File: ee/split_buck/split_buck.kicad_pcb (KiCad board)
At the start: 2 copper layers, 21.6 x 34.3 mm, 13 parts, among them J1 Conn_01x08, J3 Conn_01x03, Q1 DMP2160U

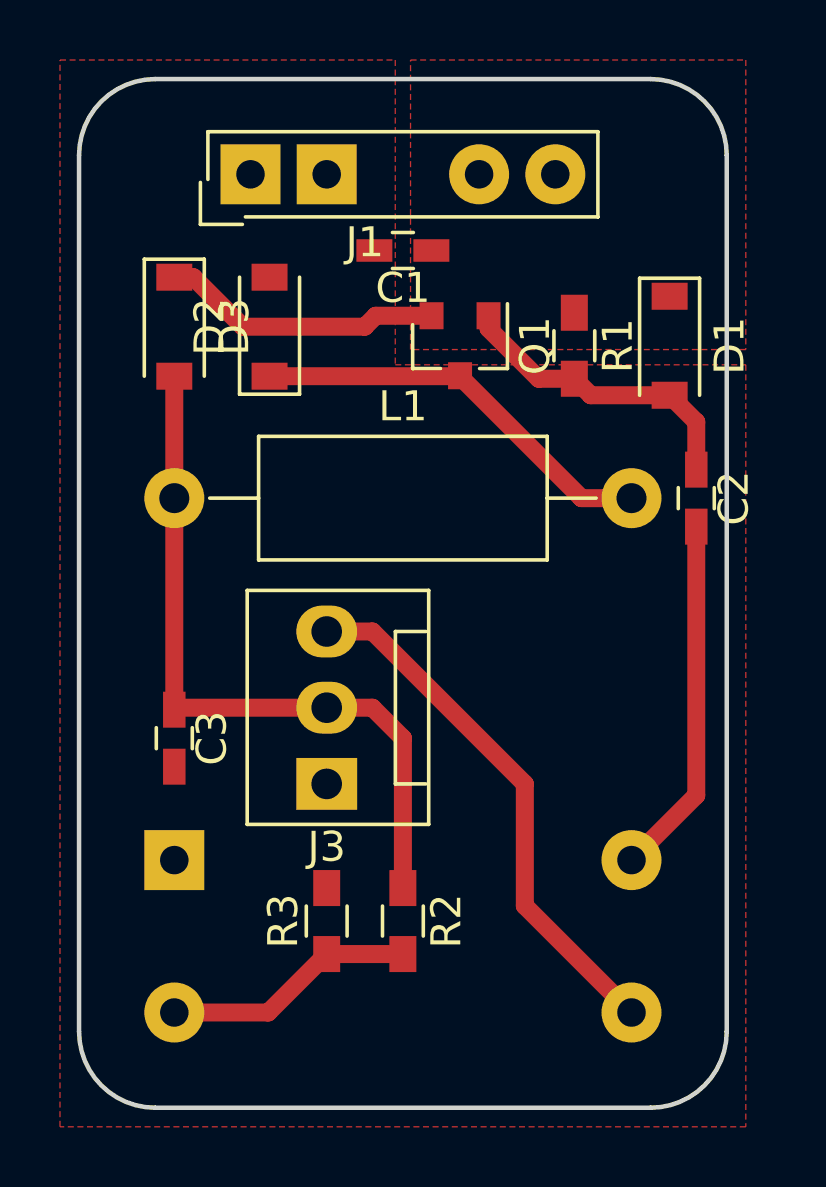
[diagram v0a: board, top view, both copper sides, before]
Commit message: Update split_buck design
- switched D1 to zener to protect FET Vgs
- increased input/output caps from 1u to 10u (0603 -> 0805)
- rotated fan header 30degrees to enable multiple channels
- added net names
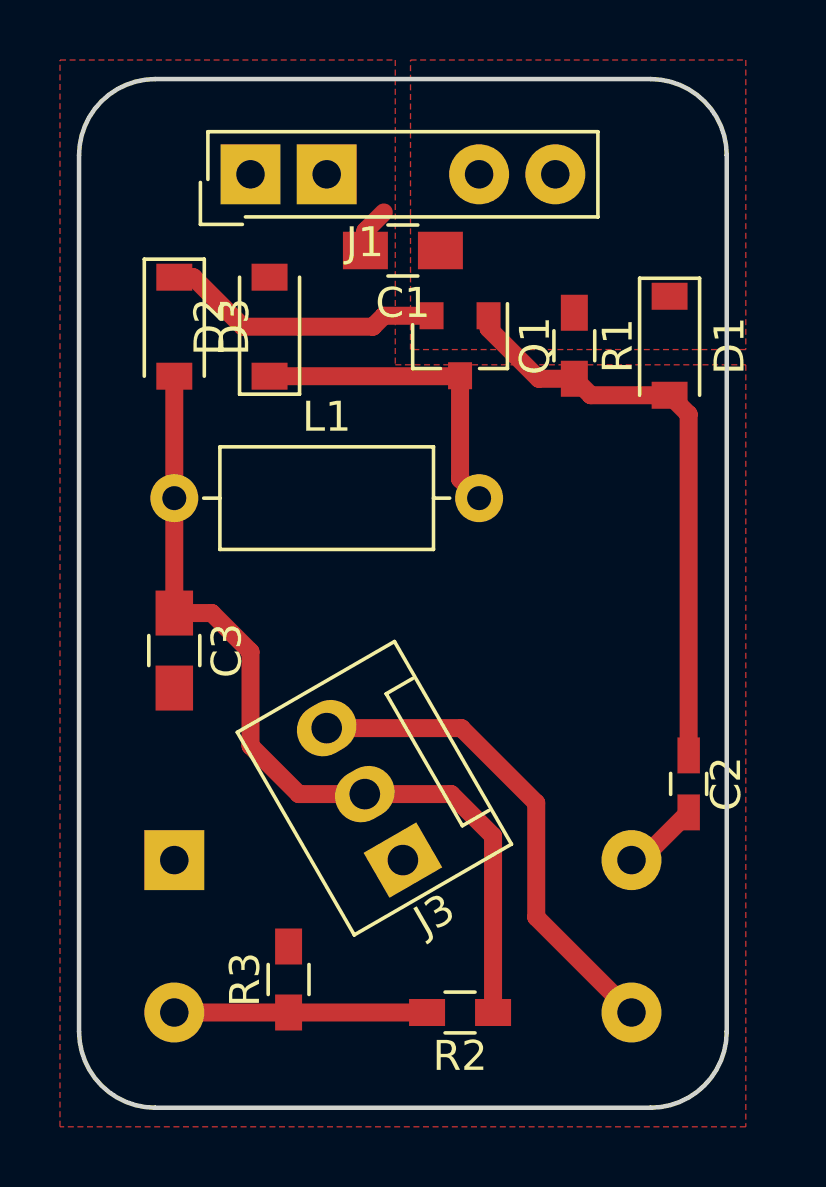
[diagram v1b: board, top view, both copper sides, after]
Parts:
- C1, C3: value 1u -> 10u; footprint Capacitors_SMD:C_0603_HandSoldering -> Capacitors_SMD:C_0805_HandSoldering
- D1: value D_Schottky -> D_Zener
- L1: footprint Inductors_THT:L_Axial_L9.5mm_D4.0mm_P15.24mm_Horizontal_Fastron_SMCC -> Inductors_THT:L_Axial_L7.0mm_D3.3mm_P10.16mm_Horizontal_Fastron_MICC
- moved C2 9.53 mm to (21.0, 24.1)
- moved R2 3.59 mm to (13.3, 31.8), turned to 180 degrees
- moved J3 3.59 mm to (11.4, 26.7), turned to 210 degrees
- moved C3 2.92 mm to (3.81, 19.7)
- moved R3 2.33 mm to (7.62, 30.6)
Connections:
- net Net-(C2-Pad1) renamed /GATE
- net Net-(C3-Pad1) renamed /FAN_VOUT
- net Net-(D2-Pad1) renamed /IND_SW
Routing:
- net /FAN_CTRL: track 12.0 -> 2.56 mm
- net /GATE: track 10.2 -> 19.7 mm
- net /FAN_VOUT: track 24.2 -> 29.3 mm
- net /IND_SW: track 13.7 -> 10.7 mm
- net GND: track 0.00 -> 1.52 mm
- net /FAN_RPM: track 17.8 -> 16.3 mm

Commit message: fine tune layout for othermill
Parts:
- moved D1 0.64 mm to (19.7, 9.53)
- moved D2 0.38 mm to (7.37, 8.89)
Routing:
- net +12V: track 9.54 -> 11.8 mm
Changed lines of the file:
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@@
     (links 26)
     (no_connects 1)
-    (area 0.559999 0.559999 22.300001 35.000001)
+    (area -0.475001 -0.475001 23.48 36.035001)
     (thickness 1.6)
     (drawings 8)
-    (tracks 37)
+    (tracks 42)
     (zones 0)
     (modules 13)
@@
   )
   (module Diodes_SMD:D_SOD-123 placed (layer F.Cu)
-    (at 20.32 9.525 270)
+    (at 19.685 9.525 270)
     (descr SOD-123)
     (tags SOD-123)
@@
   )
   (module Diodes_SMD:D_SOD-123 placed (layer F.Cu)
-    (at 6.985 8.89 90)
+    (at 7.366 8.89 90)
     (descr SOD-123)
     (tags SOD-123)
@@
   (gr_arc (start 19.685 3.175) (end 19.685 0.635) (angle 90) (layer Edge.Cuts) (width 0.15))
   (gr_arc (start 3.175 3.175) (end 0.635 3.175) (angle 90) (layer Edge.Cuts) (width 0.15))
+  (segment (start 12.385 8.525) (end 12.385 6.645) (width 0.6) (layer F.Cu) (net 1))
+  (segment (start 12.385 6.645) (end 12.68 6.35) (width 0.6) (layer F.Cu) (net 1))
   (segment (start 3.81 7.24) (end 4.446 7.24) (width 0.6) (layer F.Cu) (net 1))
   (segment (start 10.795 8.525) (end 12.385 8.525) (width 0.6) (layer F.Cu) (net 1))
@@
   (segment (start 12.235 31.75) (end 7.62 31.75) (width 0.6) (layer F.Cu) (net 3))
   (segment (start 3.81 31.75) (end 7.62 31.75) (width 0.6) (layer F.Cu) (net 3))
-  (segment (start 8.89 22.270591) (end 13.380591 22.270591) (width 0.6) (layer F.Cu) (net 4))
+  (segment (start 8.89 22.270591) (end 12.872591 22.270591) (width 0.6) (layer F.Cu) (net 4) (status 400000))
   (segment (start 15.875 28.575) (end 19.05 31.75) (width 0.6) (layer F.Cu) (net 4))
-  (segment (start 15.875 24.765) (end 15.875 28.575) (width 0.6) (layer F.Cu) (net 4))
-  (segment (start 13.380591 22.270591) (end 15.875 24.765) (width 0.6) (layer F.Cu) (net 4))
+  (segment (start 15.875 25.273) (end 15.875 28.575) (width 0.6) (layer F.Cu) (net 4))
+  (segment (start 12.872591 22.270591) (end 15.875 25.273) (width 0.6) (layer F.Cu) (net 4))
   (segment (start 19.05 26.67) (end 19.365 26.67) (width 0.6) (layer F.Cu) (net 5))
   (segment (start 19.365 26.67) (end 20.955 25.08) (width 0.6) (layer F.Cu) (net 5))
-  (segment (start 20.955 23.18) (end 20.955 11.81) (width 0.6) (layer F.Cu) (net 6))
-  (segment (start 20.955 11.81) (end 20.32 11.175) (width 0.6) (layer F.Cu) (net 6))
+  (segment (start 20.955 23.18) (end 20.955 22.733) (width 0.6) (layer F.Cu) (net 6))
+  (segment (start 20.955 22.733) (end 21.209 22.479) (width 0.6) (layer F.Cu) (net 6))
+  (segment (start 21.209 22.479) (end 21.209 12.064) (width 0.6) (layer F.Cu) (net 6))
+  (segment (start 21.209 12.064) (end 20.32 11.175) (width 0.6) (layer F.Cu) (net 6))
   (segment (start 20.32 11.175) (end 20.32 11.176) (width 0.6) (layer F.Cu) (net 6))
   (segment (start 20.32 11.175) (end 17.695 11.175) (width 0.6) (layer F.Cu) (net 6))
@@
   (segment (start 3.81 14.605) (end 3.81 18.435) (width 0.6) (layer F.Cu) (net 7))
   (segment (start 3.81 10.54) (end 3.81 14.605) (width 0.6) (layer F.Cu) (net 7))
+  (segment (start 7.366 10.54) (end 13.32 10.54) (width 0.6) (layer F.Cu) (net 8) (status C00000))
+  (segment (start 13.32 10.54) (end 13.335 10.525) (width 0.6) (layer F.Cu) (net 8) (status C00000))
   (segment (start 13.335 10.525) (end 13.335 13.97) (width 0.6) (layer F.Cu) (net 8))
   (segment (start 13.335 13.97) (end 13.97 14.605) (width 0.6) (layer F.Cu) (net 8))
-  (segment (start 6.985 10.54) (end 13.32 10.54) (width 0.6) (layer F.Cu) (net 8))
   (zone (net 1) (net_name +12V) (layer F.Cu) (hatch edge 0.508)
     (connect_pads (clearance 0.6))

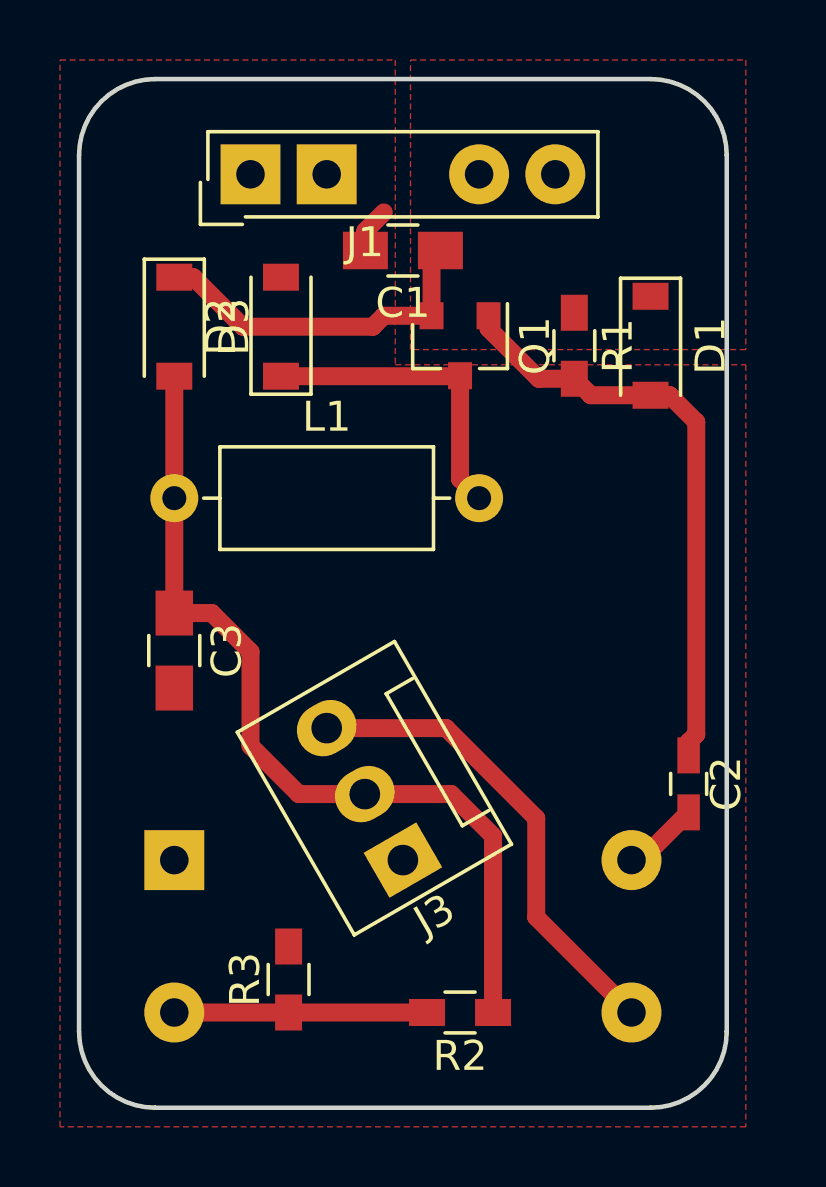
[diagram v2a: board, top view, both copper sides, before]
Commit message: update layout for carrier with new pin assignments
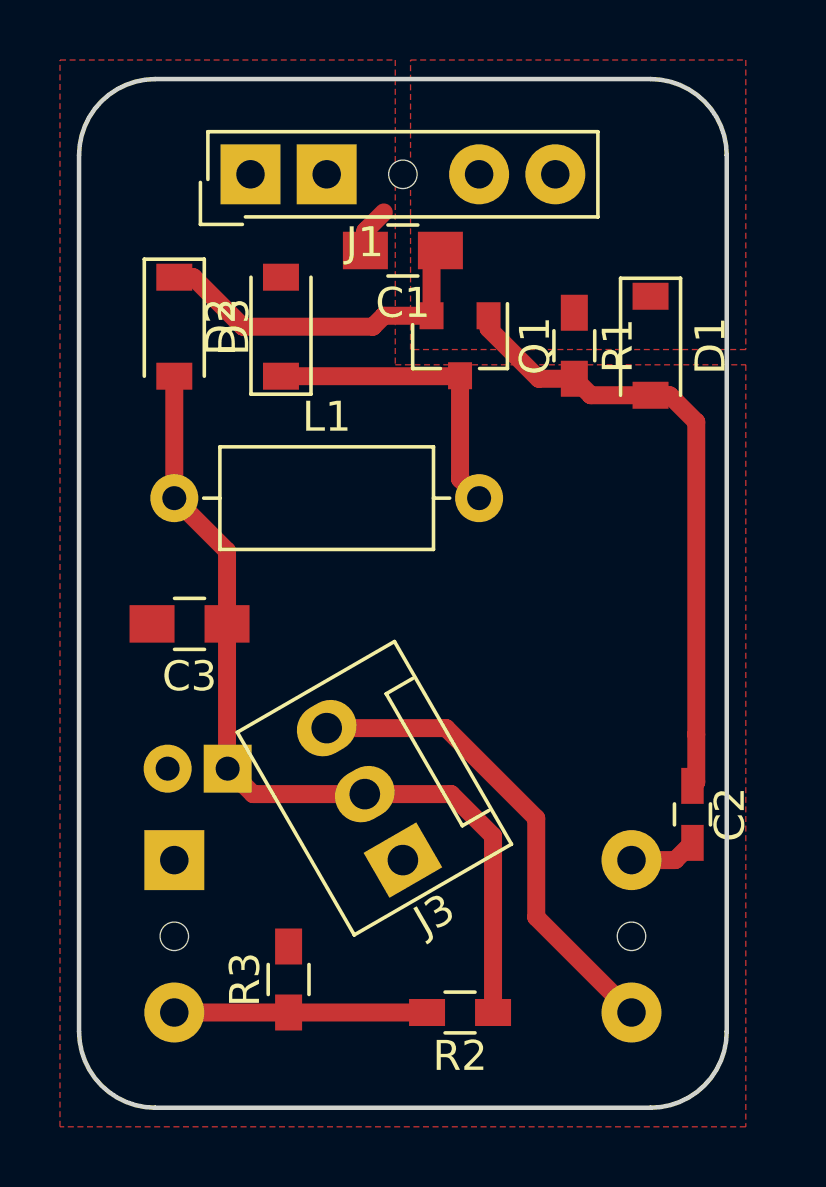
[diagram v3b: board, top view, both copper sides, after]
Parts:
- added C4: 100u, Capacitors_THT:CP_Radial_D5.0mm_P2.00mm, B.Cu at (5.59, 23.6)
- J1: footprint custom:Fan_Controller -> custom:Fan_Controller_all
- moved C2 1.02 mm to (21.1, 25.1)
- moved C3 1.02 mm to (4.32, 18.8), turned to 180 degrees
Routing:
- net /GATE: track 19.9 -> 20.8 mm
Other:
- rule trace_min: 0.2 -> 0.4
